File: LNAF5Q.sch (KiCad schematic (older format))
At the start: 25 parts, among them P1 SMA-KIT-1.5MF, U1 SWITCH, U2 SWITCH, U3 LNA, U4 SAW

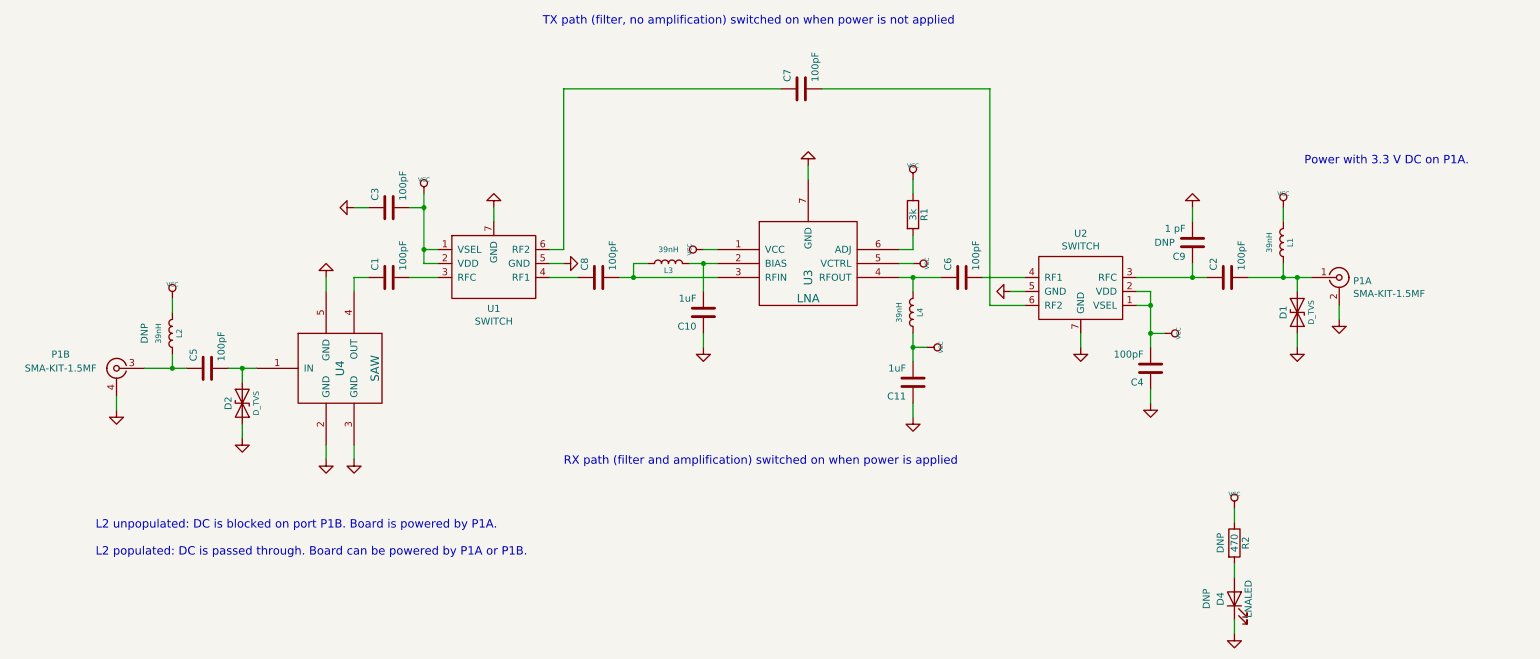
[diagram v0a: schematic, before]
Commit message: renumber capacitor reference designators
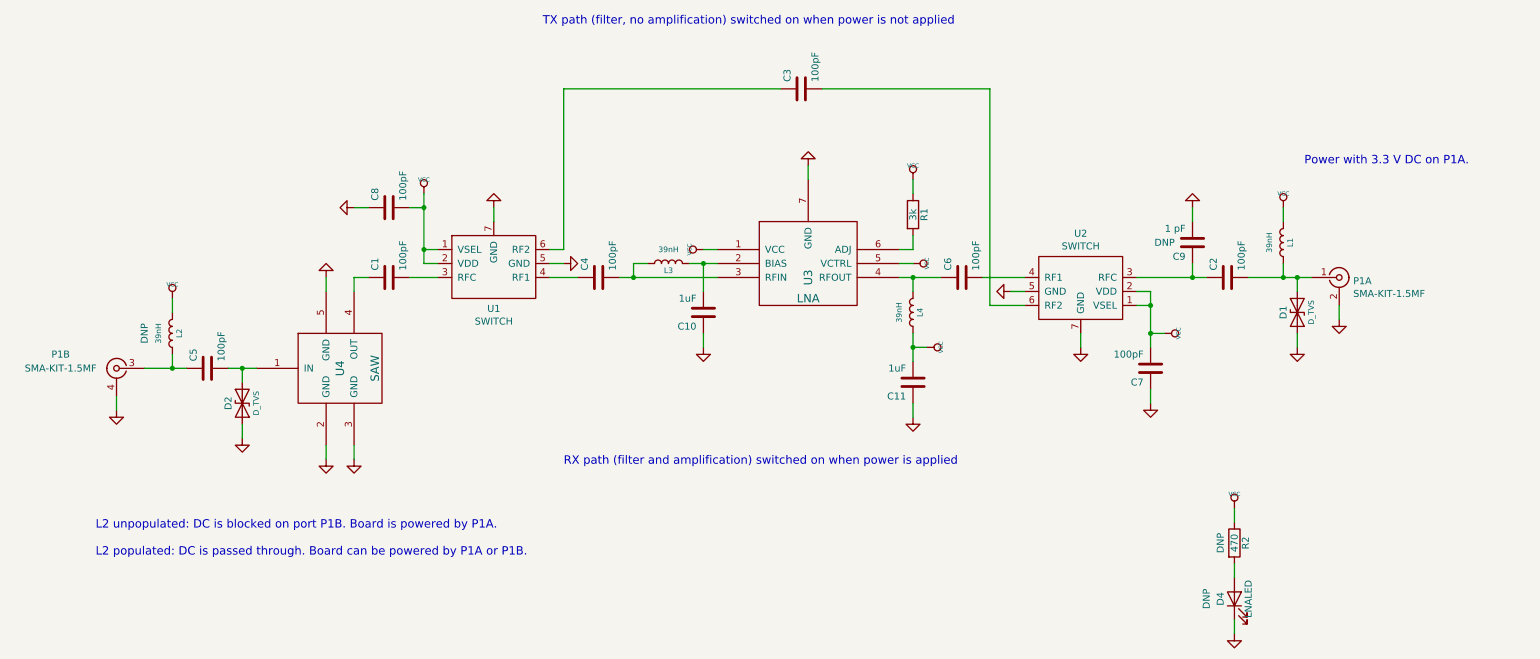
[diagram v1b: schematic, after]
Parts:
- renumbered C7 to C3, C8 to C4, C4 to C7, C3 to C8
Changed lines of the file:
@@
 Sheet 1 1
 Title "LNAF5Q"
-Date "2020-08-03"
+Date "2020-08-05"
 Rev ""
 Comp "Copyright (c) 2014-2020 Great Scott Gadgets <info@greatscottgadgets.com>"
@@
 RX path (filter and amplification) switched on when power is applied\n
 $Comp
-L Device:C C7
+L Device:C C3
 U 1 1 52F69E98
 P 6200 1900
-F 0 "C7" H 6250 2000 50  0000 L CNN
+F 0 "C3" H 6250 2000 50  0000 L CNN
 F 1 "100pF" H 6250 1800 50  0000 L CNN
 F 2 "gsg-modules:0402" H 6200 1900 50  0001 C CNN
@@
 $EndComp
 $Comp
-L Device:C C8
+L Device:C C4
 U 1 1 52F69EB1
 P 4750 3250
-F 0 "C8" H 4800 3350 50  0000 L CNN
+F 0 "C4" H 4800 3350 50  0000 L CNN
 F 1 "100pF" H 4800 3150 50  0000 L CNN
 F 2 "gsg-modules:0402" H 4750 3250 50  0001 C CNN
@@
 $EndComp
 $Comp
-L Device:C C3
+L Device:C C8
 U 1 1 5F078CB4
 P 3250 2750
-F 0 "C3" H 3300 2850 50  0000 L CNN
+F 0 "C8" H 3300 2850 50  0000 L CNN
 F 1 "100pF" H 3300 2650 50  0000 L CNN
 F 2 "gsg-modules:0402" H 3250 2750 50  0001 C CNN
@@
 $EndComp
 $Comp
-L Device:C C4
+L Device:C C7
 U 1 1 5F0987F0
 P 8700 3900
-F 0 "C4" H 8750 4000 50  0000 L CNN
+F 0 "C7" H 8750 4000 50  0000 L CNN
 F 1 "100pF" H 8750 3800 50  0000 L CNN
 F 2 "gsg-modules:0402" H 8700 3900 50  0001 C CNN

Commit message: optimize part selection for 915 MHz
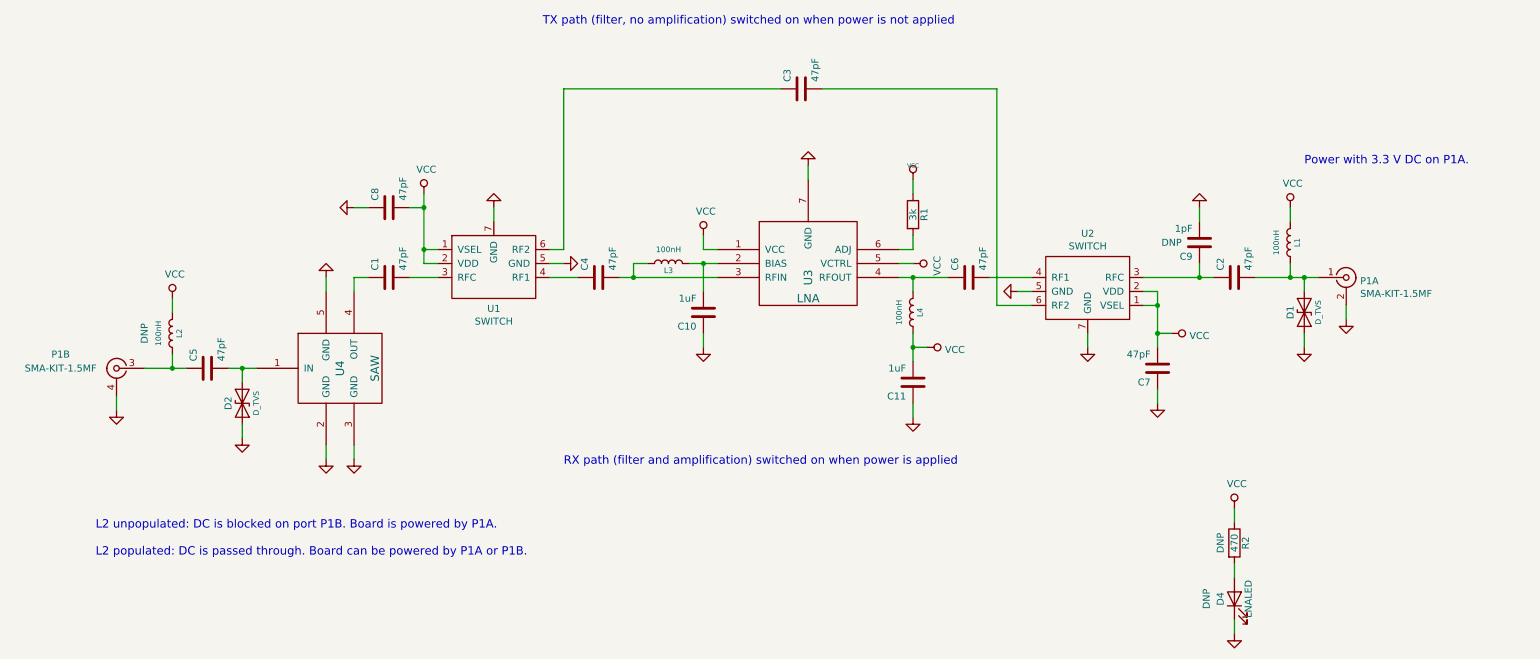
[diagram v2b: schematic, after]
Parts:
- C1, C2, C3, C4, C5, C6, C7, C8: value 100pF -> 47pF; Description CAP CER 100PF 50V 5% NP0 0402 -> CAP CER 47PF 50V C0G/NP0 0402; Part Number GCM1555C1H101JA16 -> GCM1555C1H470JA16D
- C9: value 1 pF -> 1pF
- L1, L2, L3, L4: value 39nH -> 100nH; Description INDUCTOR HI FREQ 39NH 5% 0402 -> FIXED IND 100NH 200MA 1.5 OHM; Part Number HK100539NJ-T -> HK1005R10J-T
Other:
- moved on the sheet: C2, C6, C7, C9, D1, L1, P1A, U2

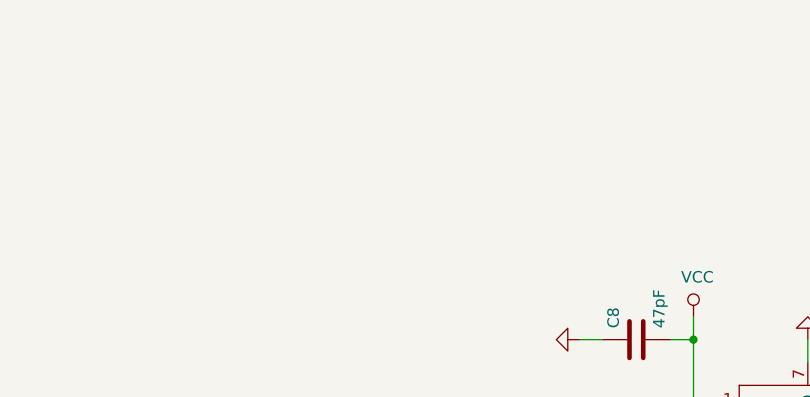
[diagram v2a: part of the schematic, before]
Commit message: document components for frequency band options
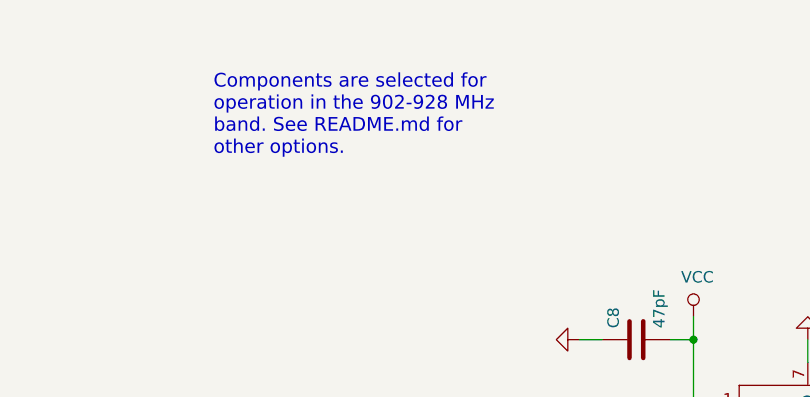
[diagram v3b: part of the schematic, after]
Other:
- note added: "Components are selected for\noperation in the 902-928 MHz\nband. See README.md for\nother options."
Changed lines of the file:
@@
 Wire Wire Line
 	7600 1900 7600 3450
+Text Notes 1400 1950 0    60   ~ 0
+Components are selected for\noperation in the 902-928 MHz\nband. See README.md for\nother options.
 $EndSCHEMATC
